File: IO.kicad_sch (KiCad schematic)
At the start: 3 parts

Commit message: added everything to repo
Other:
- note removed: "Ipsum lorem"
- note removed: "What's going on here:"
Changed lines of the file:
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@@
-		)
-	)
-	(text "Ipsum lorem\n"
-		(exclude_from_sim no)
-		(at 18.542 16.256 0)
-		(effects
-			(font
-				(size 1.27 1.27)
-				(color 132 0 0 1)
-			)
-		)
-	)
-	(text "What's going on here:\n"
-		(exclude_from_sim no)
-		(at 61.468 14.224 0)
-		(effects
-			(font
-				(size 1.905 1.905)
-				(thickness 0.381)
-				(bold yes)
-				(color 132 0 0 1)
-			)
 		)
 	)
@@
 		)
 	)
-	(polyline
-		(pts
-			(xy 12.7 34.29) (xy 118.11 34.29)
-		)
-		(stroke
-			(width 0)
-			(type dash)
-			(color 132 0 0 1)
-		)
-	)
 	(wire
 		(pts
@@
 		)
 	)
-	(polyline
-		(pts
-			(xy 118.11 12.7) (xy 118.11 34.29)
-		)
-		(stroke
-			(width 0)
-			(type dash)
-			(color 132 0 0 1)
-		)
-	)

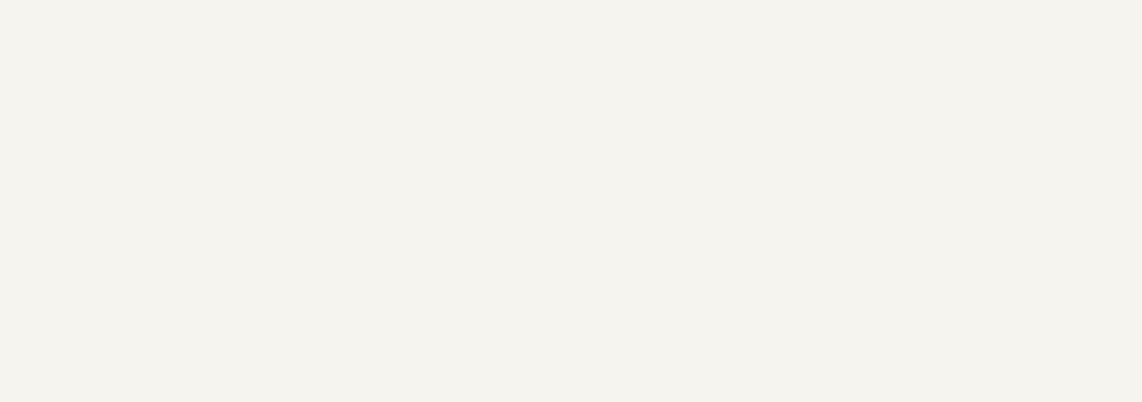
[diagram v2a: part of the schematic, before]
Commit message: text comments sections added
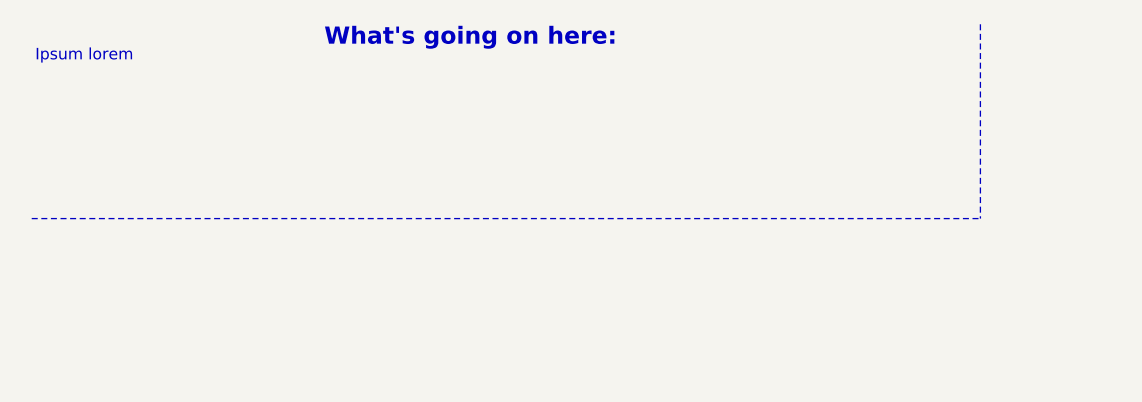
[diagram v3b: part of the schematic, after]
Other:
- note added: "Ipsum lorem"
- note added: "What's going on here:"
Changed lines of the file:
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@@
+		)
+	)
+	(text "Ipsum lorem\n"
+		(exclude_from_sim no)
+		(at 18.542 16.256 0)
+		(effects
+			(font
+				(size 1.27 1.27)
+				(color 132 0 0 1)
+			)
+		)
+	)
+	(text "What's going on here:\n"
+		(exclude_from_sim no)
+		(at 61.468 14.224 0)
+		(effects
+			(font
+				(size 1.905 1.905)
+				(thickness 0.381)
+				(bold yes)
+				(color 132 0 0 1)
+			)
 		)
 	)
@@
 		)
 	)
+	(polyline
+		(pts
+			(xy 12.7 34.29) (xy 118.11 34.29)
+		)
+		(stroke
+			(width 0)
+			(type dash)
+			(color 132 0 0 1)
+		)
+	)
 	(wire
 		(pts
@@
 		)
 	)
+	(polyline
+		(pts
+			(xy 118.11 12.7) (xy 118.11 34.29)
+		)
+		(stroke
+			(width 0)
+			(type dash)
+			(color 132 0 0 1)
+		)
+	)
